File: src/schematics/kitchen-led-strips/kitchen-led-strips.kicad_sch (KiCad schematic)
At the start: 75 parts, among them Q1 BC847BS, Q2 BC847BS, U1 DML3006LFDS, U2 AP62150WU, U3 PIC16F15355-I/MV

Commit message: Final PCB tweaks.  Generated the gerbers for fabrication.
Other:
- note added: "Maximum LED strip is 5m@14.4W/m Input is 12V_{dc}±10%, maximum 8A."
- note removed: "Maximum LED strip is 5m@14.4W/m Input is 12V_{dc}±10%, maximum 7A."
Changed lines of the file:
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@@
     (effects (font (size 1.27 1.27)) (justify left bottom))
   )
-  (text "Maximum LED strip is 5m@14.4W/m\nInput is 12V_{dc}±10%, maximum 7A."
+  (text "Maximum LED strip is 5m@14.4W/m\nInput is 12V_{dc}±10%, maximum 8A."
     (at 26.67 17.78 0)
     (effects (font (size 1.27 1.27)) (justify left bottom))

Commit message: Added the BOM and placement files for JLCPCB-with-LCSC fabrication.
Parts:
- FB1: Manufacturer2 (none) -> Walsin; Manufacturer2PartNumber (none) -> WLBD2012HCU121TH
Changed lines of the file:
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@@
+      (effects (font (size 1.27 1.27)) (justify left) hide)
+    )
+    (property "Manufacturer2" "Walsin" (id 7) (at 73.66 31.75 0)
+      (effects (font (size 1.27 1.27)) (justify left) hide)
+    )
+    (property "Manufacturer2PartNumber" "WLBD2012HCU121TH" (id 8) (at 73.66 31.75 0)
       (effects (font (size 1.27 1.27)) (justify left) hide)
     )

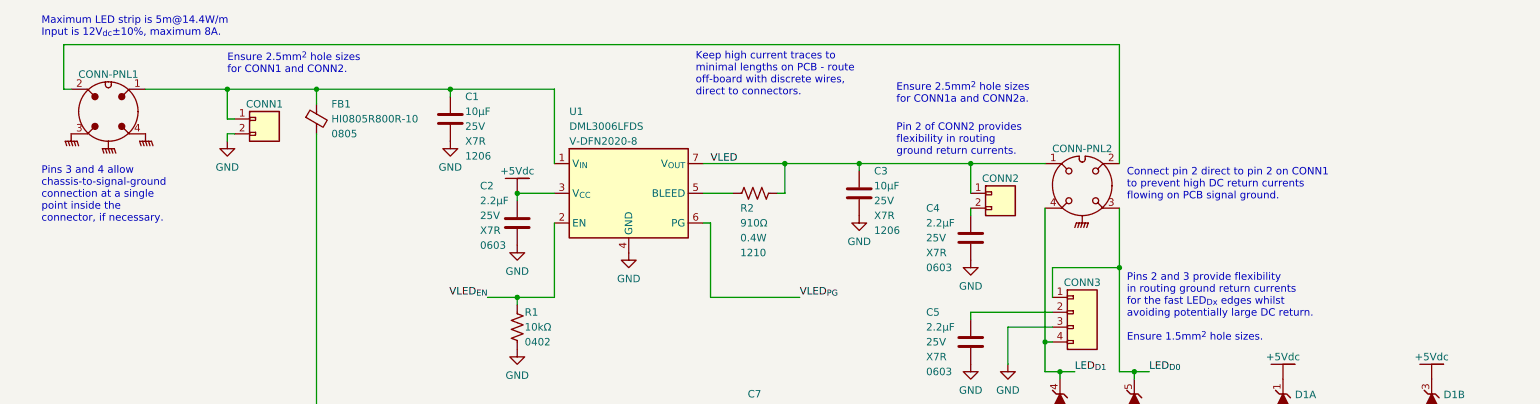
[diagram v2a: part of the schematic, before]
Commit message: Fixed some labelling errors / typos on the schematic.
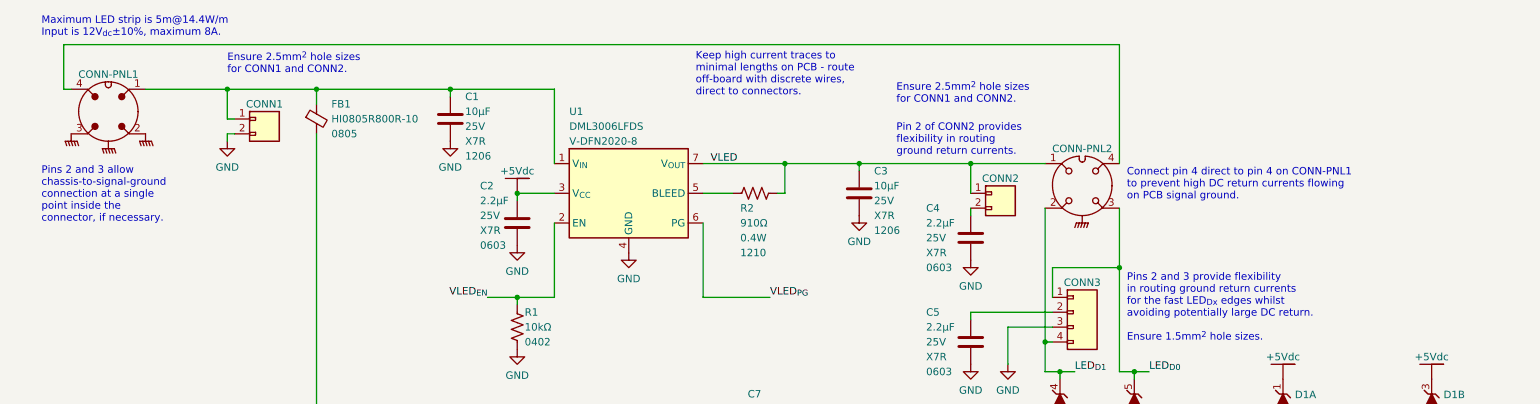
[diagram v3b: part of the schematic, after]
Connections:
- net GND: now also CONN-PNL1.2 (P2); no longer CONN-PNL1.4 (P4)
- net LED_{D1}: now also CONN-PNL2.2 (P2); no longer CONN-PNL2.4 (P4)
- new net: CONN-PNL1.4 (P4), CONN-PNL2.4 (P4)
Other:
- note added: "Connect pin 4 direct to pin 4 on CONN-PNL1 to prevent high DC return currents flowing on PCB signal ground."
- note added: "Pins 2 and 3 allow chassis-to-signal-ground connection at a single point inside the connector, if necessary."
- note removed: "Connect pin 2 direct to pin 2 on CONN1 to prevent high DC return currents flowing on PCB signal ground."
- note removed: "Ensure 2.5mm^{2} hole sizes for CONN1a and CONN2a."
- note removed: "Pins 3 and 4 allow chassis-to-signal-ground connection at a single point inside the connector, if necessary."
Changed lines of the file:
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@@
     (stroke (width 0) (type default) (color 0 0 0 0))
   )
-  (wire (pts (xy 140.97 49.53) (xy 140.97 62.23))
+  (wire (pts (xy 139.7 49.53) (xy 139.7 62.23))
     (stroke (width 0) (type default) (color 0 0 0 0))
   )
@@
     (stroke (width 0) (type default) (color 0 0 0 0))
   )
-  (wire (pts (xy 140.97 62.23) (xy 156.21 62.23))
+  (wire (pts (xy 139.7 62.23) (xy 151.13 62.23))
     (stroke (width 0) (type default) (color 0 0 0 0))
   )
@@
   )
   (wire (pts (xy 30.48 26.67) (xy 31.75 26.67))
-    (stroke (width 0) (type default) (color 0 0 0 0))
-  )
-  (wire (pts (xy 139.7 49.53) (xy 140.97 49.53))
     (stroke (width 0) (type default) (color 0 0 0 0))
   )
@@
     (effects (font (size 1.27 1.27)) (justify left bottom))
   )
-  (text "Connect pin 2 direct to pin 2 on CONN1\nto prevent high DC return currents\nflowing on PCB signal ground."
+  (text "Connect pin 4 direct to pin 4 on CONN-PNL1\nto prevent high DC return currents flowing\non PCB signal ground."
     (at 212.09 45.72 0)
     (effects (font (size 1.27 1.27)) (justify left bottom))
@@
     (effects (font (size 1.27 1.27)) (justify left bottom))
   )
-  (text "Ensure 2.5mm^{2} hole sizes\nfor CONN1a and CONN2a."
-    (at 172.72 29.21 0)
-    (effects (font (size 1.27 1.27)) (justify left bottom))
-  )
-  (text "Pins 3 and 4 allow\nchassis-to-signal-ground\nconnection at a single\npoint inside the\nconnector, if necessary."
+  (text "Ensure 2.5mm^{2} hole sizes\nfor CONN1 and CONN2." (at 172.72 29.21 0)
+    (effects (font (size 1.27 1.27)) (justify left bottom))
+  )
+  (text "Pins 2 and 3 allow\nchassis-to-signal-ground\nconnection at a single\npoint inside the\nconnector, if necessary."
     (at 26.67 49.53 0)
     (effects (font (size 1.27 1.27)) (justify left bottom))
@@
     (effects (font (size 1.27 1.27)) (justify left bottom))
   )
-  (label "VLED_{PG}" (at 156.21 62.23 0)
-    (effects (font (size 1.27 1.27)) (justify left bottom))
-  )
+  (label "VLED_{PG}" (at 151.13 62.23 0)
+    (effects (font (size 1.27 1.27)) (justify left bottom))
+  )
